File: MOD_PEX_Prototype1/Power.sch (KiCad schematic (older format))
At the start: 15 parts, among them U2 AP1117E50G, U3 AP1117E33G

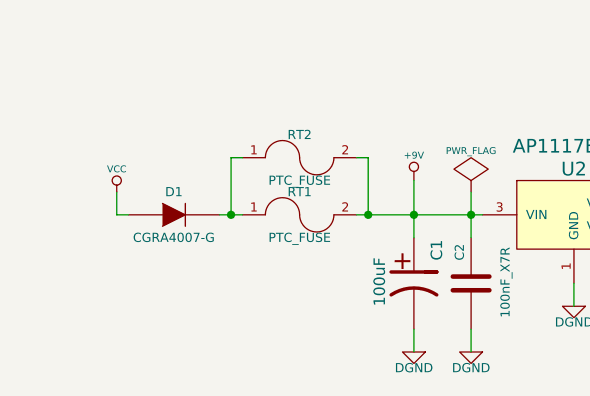
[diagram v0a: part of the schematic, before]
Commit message: updating control chain circuit
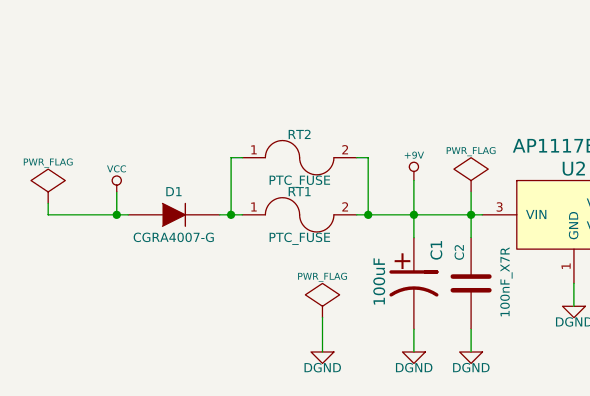
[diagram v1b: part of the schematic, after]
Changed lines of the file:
@@
 	2750 3400 2750 3500
 Wire Wire Line
-	2750 3500 2800 3500
+	2450 3500 2800 3500
 $Comp
 L LINEAR_REGULATOR_SOT223_3 U3
@@
 	3250 3250 3250 3500
 Connection ~ 3250 3500
+$Comp
+L PWR_FLAG #FLG028
+U 1 1 54B500E8
+P 3650 3950
+F 0 "#FLG028" H 3650 4045 30  0001 C CNN
+F 1 "PWR_FLAG" H 3650 4130 30  0000 C CNN
+F 2 "" H 3650 3950 60  0000 C CNN
+F 3 "" H 3650 3950 60  0000 C CNN
+	1    3650 3950
+	1    0    0    -1
+$EndComp
+$Comp
+L DGND #PWR029
+U 1 1 54B50120
+P 3650 4100
+F 0 "#PWR029" H 3650 4100 40  0001 C CNN
+F 1 "DGND" H 3650 4030 40  0000 C CNN
+F 2 "" H 3650 4100 60  0000 C CNN
+F 3 "" H 3650 4100 60  0000 C CNN
+	1    3650 4100
+	-1   0    0    -1
+$EndComp
+Wire Wire Line
+	3650 3950 3650 4100
+$Comp
+L PWR_FLAG #FLG030
+U 1 1 54B50E4C
+P 2450 3450
+F 0 "#FLG030" H 2450 3545 30  0001 C CNN
+F 1 "PWR_FLAG" H 2450 3630 30  0000 C CNN
+F 2 "" H 2450 3450 60  0000 C CNN
+F 3 "" H 2450 3450 60  0000 C CNN
+	1    2450 3450
+	1    0    0    -1
+$EndComp
+Wire Wire Line
+	2450 3450 2450 3500
+Connection ~ 2750 3500
 $EndSCHEMATC
